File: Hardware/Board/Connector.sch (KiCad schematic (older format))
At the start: 8 parts, among them J10 WAGO_Klemmleiste_8-pol, J11 RJ12, J12 RJ45, J13 WAGO_Klemmleiste_6-pol, J2 Conn_02x25_Odd_Even, J7 WAGO_Klemmleiste_6-pol, J8 WAGO_Klemmleiste_4-pol, J9 WAGO_Klemmleiste_8-pol

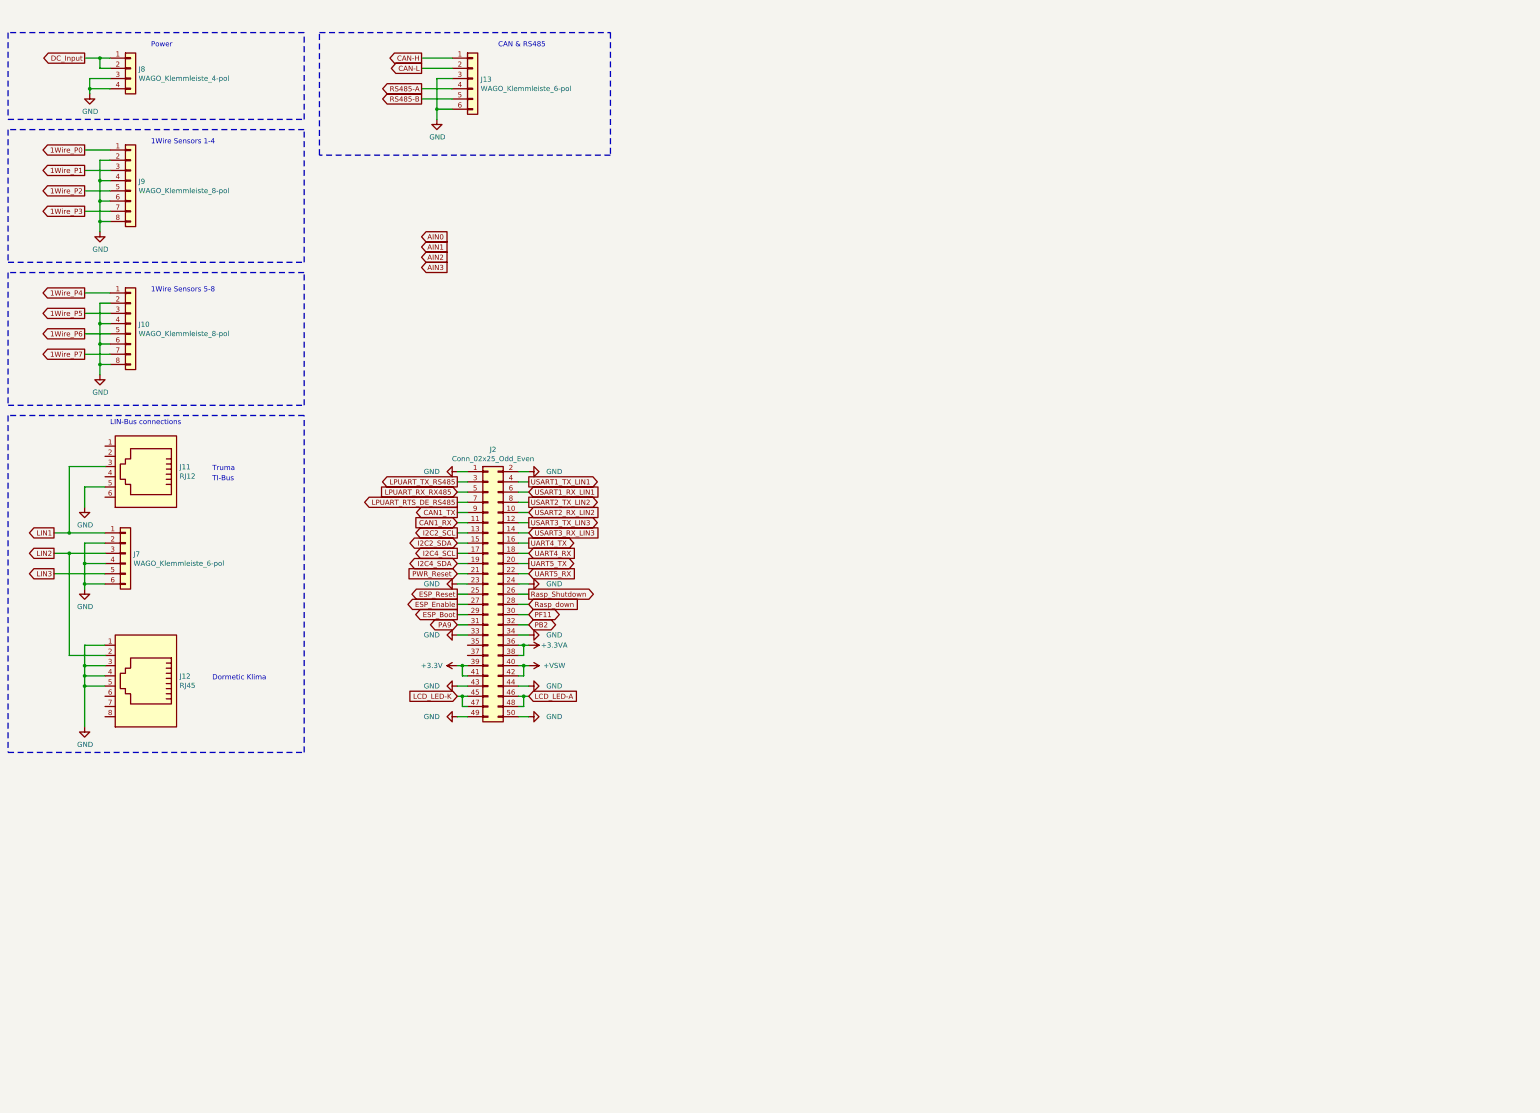
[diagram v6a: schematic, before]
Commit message: MCU Section fertig, Analog Inputs angelegt, Schaltplan neu organisiert, alte Datenblätter entfernt.
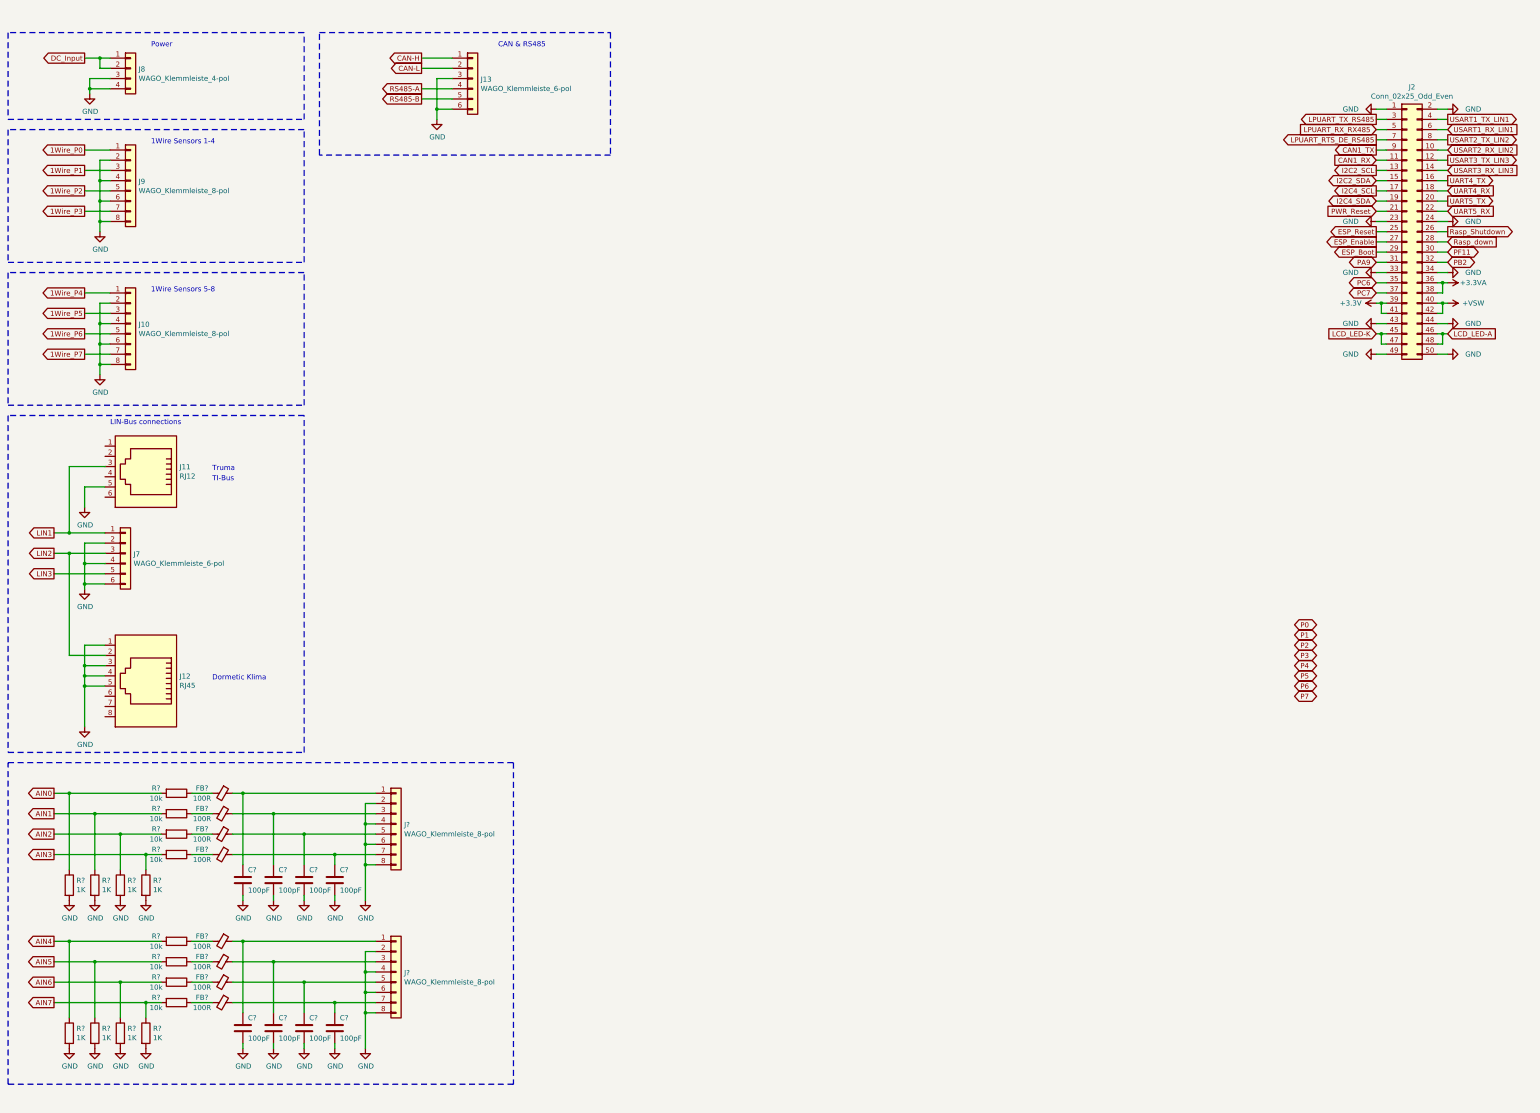
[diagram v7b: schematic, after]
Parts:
- added C? (x8): 100pF, Capacitor_SMD:C_0603_1608Metric, symbol Device:C
- added FB? (x8): 100R, Inductor_SMD:L_0603_1608Metric, symbol Device:Ferrite_Bead_Small
- added J? (x2): WAGO_Klemmleiste_8-pol, TerminalBlock_WAGO:TerminalBlock_WAGO_236-108_1x08_P5.00mm_45Degree, symbol Womo-rescue:WAGO_Klemmleiste_8-pol-WAGO_Klemmleisten
- added R? (x8): 1K, Resistor_SMD:R_0603_1608Metric, symbol Device:R
- added R? (x8): 10k, Resistor_SMD:R_0603_1608Metric, symbol Device:R
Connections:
- net AIN0: now also R?.1, R?.2
- net AIN1: now also R?.1, R?.2
- net AIN2: now also R?.1, R?.2
- net AIN3: now also R?.1, R?.2
- net GND: now also C?.2, C?.2, C?.2, C?.2, C?.2, C?.2, C?.2, C?.2, J?.2 (Pin_2), J?.2 (Pin_2), J?.4 (Pin_4), J?.4 (Pin_4), J?.6 (Pin_6), J?.6 (Pin_6), J?.8 (Pin_8), J?.8 (Pin_8), R?.2, R?.2, R?.2, R?.2, R?.2, R?.2, R?.2, R?.2
- net PC6: now reaches J2.35 (Pin_35)
- net PC7: now reaches J2.37 (Pin_37)
- new net: C?.1, FB?.1, J?.1 (Pin_1) (x2)
- new net: C?.1, FB?.1, J?.3 (Pin_3) (x2)
- new net: C?.1, FB?.1, J?.5 (Pin_5) (x2)
- new net: C?.1, FB?.1, J?.7 (Pin_7) (x2)
- new net: FB?.2, R?.1 (x8)
- new net AIN4: R?.1, R?.2
- new net AIN5: R?.1, R?.2
- new net AIN6: R?.1, R?.2
- new net AIN7: R?.1, R?.2
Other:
- moved on the sheet: J2

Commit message: Trennung MCU und Rest, Footprints fast alles zugewiesen, GSM Modul integriert, viel Kleinkram
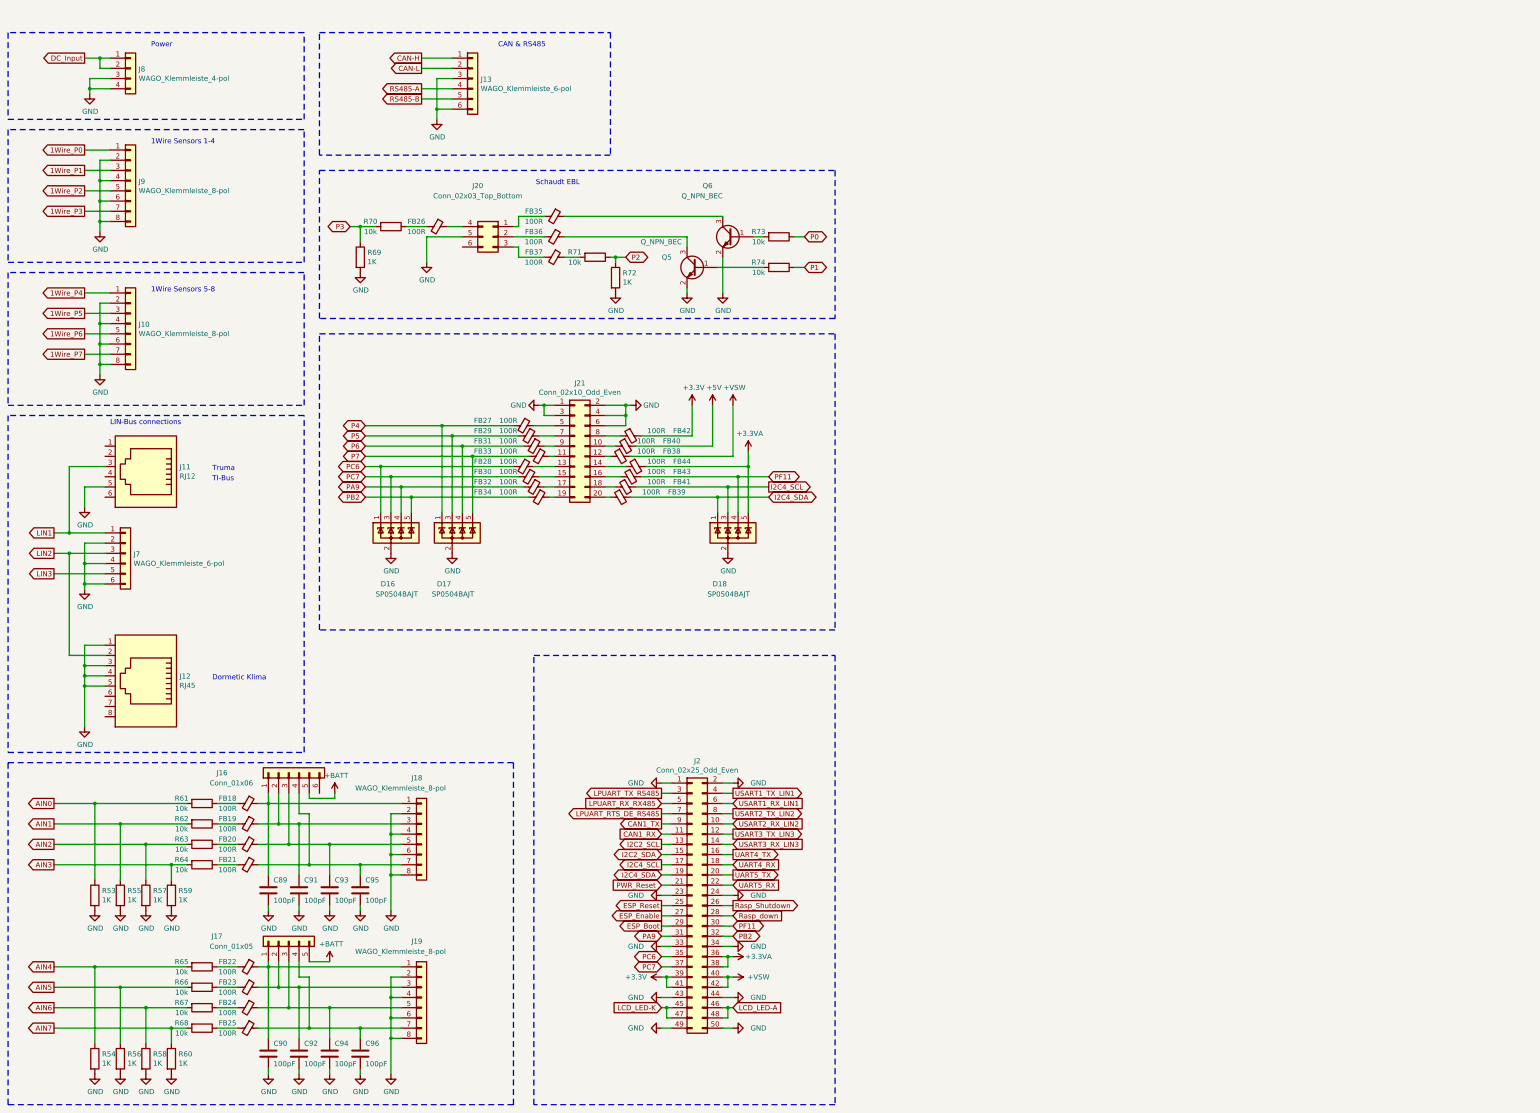
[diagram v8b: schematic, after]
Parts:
- added D16, D17, D18: SP0504BAJT, Package_TO_SOT_SMD:SOT-353_SC-70-5, symbol Power_Protection:SP0504BAJT
- added FB26, FB27, FB28, FB29, FB30, FB31, FB32, FB33, FB34, FB35, FB36, FB37, FB38, FB39, FB40, FB41, FB42, FB43, FB44: 100R, Inductor_SMD:L_0603_1608Metric, symbol Device:Ferrite_Bead_Small
- added J16: Conn_01x06, symbol Connector_Generic:Conn_01x06
- added J17: Conn_01x05, symbol Connector_Generic:Conn_01x05
- added J20: Conn_02x03_Top_Bottom, Connectors_Molex:Molex_Microfit3_Header_02x03_Straight_43045-0628, symbol Connector_Generic:Conn_02x03_Top_Bottom
- added J21: Conn_02x10_Odd_Even, Connector_PinHeader_2.54mm:PinHeader_2x10_P2.54mm_Vertical, symbol Connector_Generic:Conn_02x10_Odd_Even
- added Q5, Q6: Q_NPN_BEC, symbol stmbl:Q_NPN_BEC
- added R69, R72: 1K, Resistor_SMD:R_0603_1608Metric, symbol Device:R
- added R70, R71, R73, R74: 10k, Resistor_SMD:R_0603_1608Metric, symbol Device:R
- J10, J9: footprint TerminalBlock_WAGO:TerminalBlock_WAGO_236-108_1x08_P5.00mm_45Degree -> WAGO Klemmleisten:WAGO_Klemmleiste_Hebel4mm²Vertikal_RM5mm_8-pol
- J11: footprint (none) -> Connector_RJ:RJ12_Amphenol_54601
- J12: footprint (none) -> Connector_RJ:RJ45_Amphenol_54602-x08_Horizontal
- J13, J7: footprint TerminalBlock_WAGO:TerminalBlock_WAGO_236-106_1x06_P5.00mm_45Degree -> WAGO Klemmleisten:WAGO_Klemmleiste_Hebel4mm²Vertikal_RM5mm_6-pol
- J18, J19: renamed from J?; footprint TerminalBlock_WAGO:TerminalBlock_WAGO_236-108_1x08_P5.00mm_45Degree -> WAGO Klemmleisten:WAGO_Klemmleiste_Hebel4mm²Vertikal_RM5mm_8-pol
- J8: footprint TerminalBlock_WAGO:TerminalBlock_WAGO_236-304_1x04_P10.00mm_45Degree -> WAGO Klemmleisten:WAGO_Klemmleiste_Hebel4mm²Vertikal_RM5mm_4-pol
- gave numbers to parts that had none: 32
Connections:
- net +3.3VA: now also D18.5 (K), FB44.2
- net +3V3: now also FB42.2
- net +VSW: now also FB38.2
- net GND: now also D16.2 (A), D17.2 (A), D18.2 (A), J20.5 (Pin_5), J21.1 (Pin_1), J21.2 (Pin_2), J21.3 (Pin_3), J21.4 (Pin_4), J21.6 (Pin_6), Q5.2 (E), Q6.2 (E), R69.2, R72.2
- net I2C4_SCL: now also D18.3 (K), FB41.2
- net I2C4_SDA: now also D18.1 (K), FB39.2
- net P0: now also R73.1
- net P1: now also R74.1
- net P2: now also R71.1, R72.1
- net P3: now also R69.1, R70.2
- net P4: now also D17.1 (K), FB27.2
- net P5: now also D17.3 (K), FB29.2
- net P6: now also D17.4 (K), FB31.2
- net P7: now also D17.5 (K), FB33.2
- net PA9: now also D16.4 (K), FB32.2
- net PB2: now also D16.5 (K), FB34.2
- net PC6: now also D16.1 (K), FB28.2
- net PC7: now also D16.3 (K), FB30.2
- net PF11: now also D18.4 (K), FB43.2
- net at C89.1, FB18.1, J18.1 (Pin_1): now also J16.1 (Pin_1)
- net at C91.1, FB19.1, J18.3 (Pin_3): now also J16.2 (Pin_2)
- net at C93.1, FB20.1, J18.5 (Pin_5): now also J16.3 (Pin_3)
- net at C95.1, FB21.1, J18.7 (Pin_7): now also J16.4 (Pin_4)
- net at C90.1, FB22.1, J19.1 (Pin_1): now also J17.1 (Pin_1)
- net at C92.1, FB23.1, J19.3 (Pin_3): now also J17.2 (Pin_2)
- net at C94.1, FB24.1, J19.5 (Pin_5): now also J17.3 (Pin_3)
- net at C96.1, FB25.1, J19.7 (Pin_7): now also J17.4 (Pin_4)
- new net: FB40.1, J21.10 (Pin_10)
- new net: FB33.1, J21.11 (Pin_11)
- new net: FB38.1, J21.12 (Pin_12)
- new net: FB28.1, J21.13 (Pin_13)
- new net: FB44.1, J21.14 (Pin_14)
- new net: FB30.1, J21.15 (Pin_15)
- new net: FB43.1, J21.16 (Pin_16)
- new net: FB32.1, J21.17 (Pin_17)
- new net: FB41.1, J21.18 (Pin_18)
- new net: FB34.1, J21.19 (Pin_19)
- new net: FB39.1, J21.20 (Pin_20)
- new net: FB27.1, J21.5 (Pin_5)
- new net: FB29.1, J21.7 (Pin_7)
- new net: FB42.1, J21.8 (Pin_8)
- new net: FB31.1, J21.9 (Pin_9)
- new net: FB35.2, J20.1 (Pin_1)
- new net: FB36.2, J20.2 (Pin_2)
- new net: FB37.2, J20.3 (Pin_3)
- new net: FB26.1, J20.4 (Pin_4)
- new net: FB26.2, R70.1
- new net: FB37.1, R71.2
- new net: FB35.1, Q6.3 (C)
- new net: FB36.1, Q5.3 (C)
- new net: Q6.1 (B), R73.2
- new net: Q5.1 (B), R74.2
- new net +5V: FB40.2
- new net +BATT: J16.5 (Pin_5), J17.5 (Pin_5)
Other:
- note added: "Schaudt EBL"
- moved on the sheet: C89, C90, C91, C92, C93, C94, C95, C96, FB18, FB19, FB20, FB21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
